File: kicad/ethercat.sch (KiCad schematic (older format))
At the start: 94 parts, among them J401 RJHSE-5384, J402 RJHSE-5384, U401 CAT24C16WI, U402 DP83822, U403 DP83822

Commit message: changing single row terminal block to double row
I've changed to double row all the connectors, RJ45 and terminal blocks,
I saves spaces and also make it more intuitive related to user
interface..lets go
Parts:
- removed C434, C435: 4700pF, servo:C_0603_1608Metric, symbol servo:Capacitor
- removed J401, J402: RJHSE-5384, Connector_RJ:RJ45_Amphenol_RJHSE538X, symbol servo:RJHSE-5384
- removed R443, R447, R448: 75e, Resistor_SMD:R_0603_1608Metric, symbol servo:Resistor
- removed R446: 470, Resistor_SMD:R_0603_1608Metric, symbol servo:Resistor
- removed TR401, TR402: S558-5500-25-F, Transformer_SMD:Transformer_Ethernet_HALO_TG111-MSC13, symbol servo:S558-5500-25-F
- added U404: rj45x2, servo:rj45x2_0845-2G1T-H5, symbol servo:rj45x2_0845-2G1T-H5
- R441: value 75e -> 470; ValueDisplayed 49.9 -> 470
- renumbered C417 to C414, C414 to C415, C415 to C416, C416 to C417, R444 to R445, R445 to R446
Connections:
- wire segments 418 -> 410
- no-connect marks 16 -> 8
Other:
- moved on the sheet: R445, R446

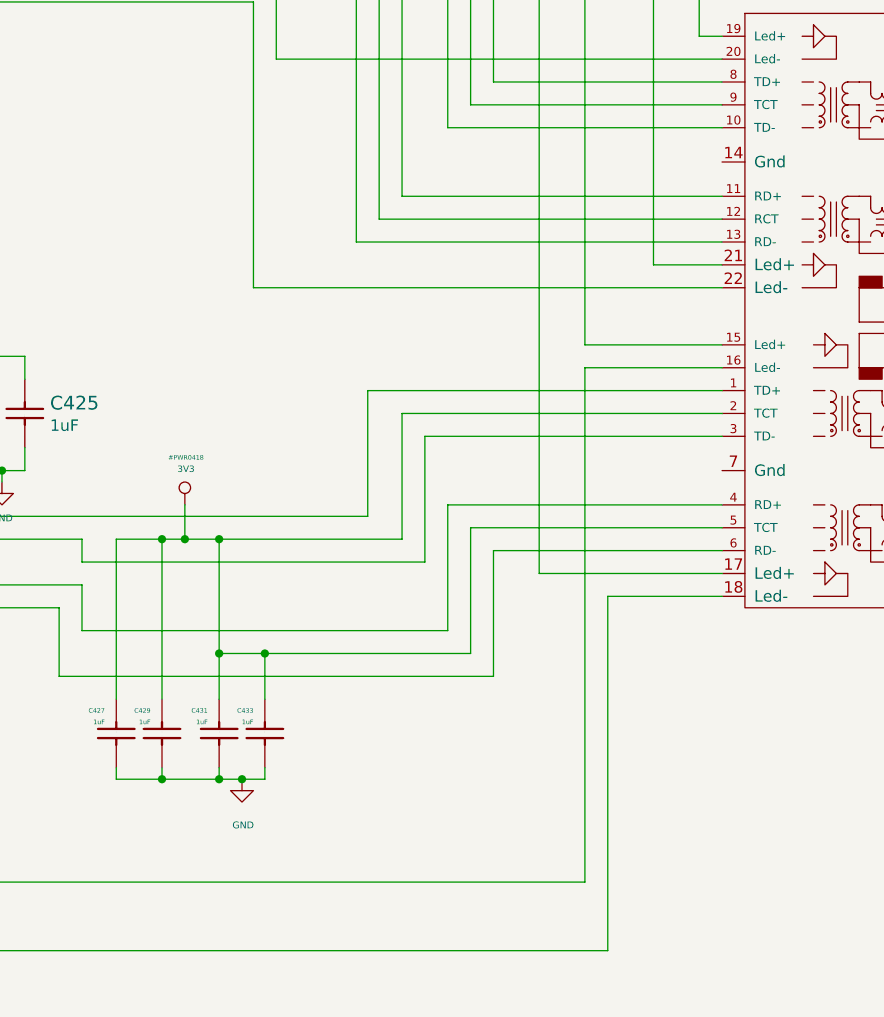
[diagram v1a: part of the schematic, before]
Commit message: added some 3d models, elminating 15vc and 2 lems
I've elminated 15vc 'cause I don't use these voltage, so I'd change 20w
15v heating power to 10w 5v more efficiency voltage to drive 3.3 and
1.2v to the core and logic. I've also elminated 2 LEMS 'cause space..
even thought there remain 3 for each motor.. more than necesary...keep
going
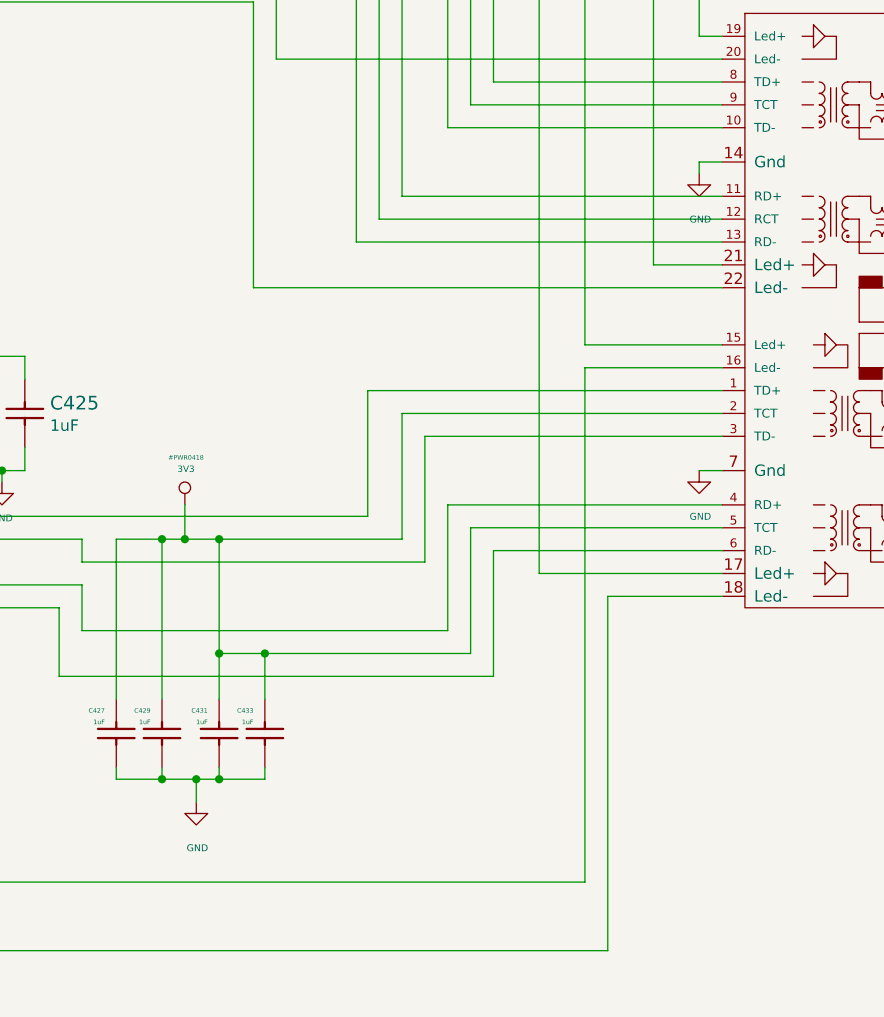
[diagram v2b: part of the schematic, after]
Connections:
- net GND: now also U404.14 (Gnd), U404.7 (Gnd)
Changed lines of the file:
@@
 L servo:GND #GND_0419
 U 1 1 6322EF1B
-P 12100 6950
-F 0 "#GND_0419" H 12105 6801 20  0001 C CNN
-F 1 "GND" H 12105 6749 30  0000 C CNN
-F 2 "" H 12100 6950 70  0000 C CNN
-F 3 "" H 12100 6950 70  0000 C CNN
-	1    12100 6950
+P 11900 7050
+F 0 "#GND_0419" H 11905 6901 20  0001 C CNN
+F 1 "GND" H 11905 6849 30  0000 C CNN
+F 2 "" H 11900 7050 70  0000 C CNN
+F 3 "" H 11900 7050 70  0000 C CNN
+	1    11900 7050
 	1    0    0    -1
 $EndComp
@@
 	2500 6100 2400 6100
 Wire Wire Line
-	12000 6950 12100 6950
-Wire Wire Line
 	12000 6400 12200 6400
 Connection ~ 12200 6400
-Connection ~ 12100 6950
-Wire Wire Line
-	12100 6950 12200 6950
-Wire Wire Line
-	12000 6950 11750 6950
+Wire Wire Line
+	12000 6950 11900 6950
 Wire Wire Line
 	11550 6950 11550 6900
@@
 Wire Wire Line
 	11150 2350 12600 2350
+Wire Wire Line
+	12000 6950 12200 6950
+Wire Wire Line
+	11900 7050 11900 6950
+Connection ~ 11900 6950
+Wire Wire Line
+	11900 6950 11750 6950
+$Comp
+L servo:GND #GND_0101
+U 1 1 5E6C77D4
+P 14100 5600
+F 0 "#GND_0101" H 14105 5451 20  0001 C CNN
+F 1 "GND" H 14105 5399 30  0000 C CNN
+F 2 "" H 14100 5600 70  0000 C CNN
+F 3 "" H 14100 5600 70  0000 C CNN
+	1    14100 5600
+	1    0    0    -1
+$EndComp
+Wire Wire Line
+	14200 5600 14100 5600
+$Comp
+L servo:GND #GND_0102
+U 1 1 5E71B6E0
+P 14100 4300
+F 0 "#GND_0102" H 14105 4151 20  0001 C CNN
+F 1 "GND" H 14105 4099 30  0000 C CNN
+F 2 "" H 14100 4300 70  0000 C CNN
+F 3 "" H 14100 4300 70  0000 C CNN
+	1    14100 4300
+	1    0    0    -1
+$EndComp
+Wire Wire Line
+	14200 4250 14100 4250
+Wire Wire Line
+	14100 4250 14100 4300
 $EndSCHEMATC

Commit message: I've reducede the PCB size ADC TVS, USB host and IDC out
TVS for ADC protection, USB out 'cause it's almost free and IDC debug
out in an IDC. Better and thinner terminal block connector help in
reduce the board size.
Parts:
- added C434: 4n7, servo:C_0603_1608Metric, symbol servo:Capacitor
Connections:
- net GND: now also C434.1; no longer U404.14 (Gnd), U404.7 (Gnd)
- new net Earth: C434.2 (Capacitor), U404.14 (Gnd), U404.7 (Gnd)
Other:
- note added: "OJO con el GND y el EARTH SPERAR"
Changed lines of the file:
@@
 Wire Wire Line
 	11900 6950 11750 6950
+Text Notes 1800 14750 0    787  ~ 157
+OJO con el GND y el EARTH SPERAR
 $Comp
-L servo:GND #GND_0101
-U 1 1 5E6C77D4
-P 14100 5600
-F 0 "#GND_0101" H 14105 5451 20  0001 C CNN
-F 1 "GND" H 14105 5399 30  0000 C CNN
-F 2 "" H 14100 5600 70  0000 C CNN
-F 3 "" H 14100 5600 70  0000 C CNN
-	1    14100 5600
+L servo:Earth #PWR?
+U 1 1 5E2B8CFA
+P 14600 6750
+AR Path="/5DC3DC9E/5E2B8CFA" Ref="#PWR?"  Part="1"
+AR Path="/5DC4A59D/5E2B8CFA" Ref="#PWR0130"  Part="1"
+F 0 "#PWR0130" H 14600 6500 20  0001 C CNN
+F 1 "Earth" H 14600 6585 39  0000 C CNN
+F 2 "" H 14600 6750 50  0001 C CNN
+F 3 "~" H 14600 6750 50  0001 C CNN
+	1    14600 6750
 	1    0    0    -1
 $EndComp
 Wire Wire Line
-	14200 5600 14100 5600
+	14000 5600 14200 5600
+Wire Wire Line
+	14000 4250 14200 4250
+$Comp
+L servo:Capacitor C434
+U 1 1 5E3BA4D2
+P 14850 6500
+F 0 "C434" V 14800 6450 20  0000 R CNN
+F 1 "4n7" V 14850 6450 20  0000 R CNN
+F 2 "servo:C_0603_1608Metric" H 14850 6400 60  0001 C CNN
+F 3 "" H 14850 6500 60  0000 C CNN
+F 4 "1uF" V 2750 7000 60  0001 C CNN "ValueDisplayed"
+	1    14850 6500
+	0    1    1    0
+$EndComp
 $Comp
 L servo:GND #GND_0102
-U 1 1 5E71B6E0
-P 14100 4300
-F 0 "#GND_0102" H 14105 4151 20  0001 C CNN
-F 1 "GND" H 14105 4099 30  0000 C CNN
-F 2 "" H 14100 4300 70  0000 C CNN
-F 3 "" H 14100 4300 70  0000 C CNN
-	1    14100 4300
+U 1 1 5E463A14
+P 14850 6750
+F 0 "#GND_0102" H 14855 6601 20  0001 C CNN
+F 1 "GND" H 14850 6593 30  0000 C CNN
+F 2 "" H 14850 6750 70  0000 C CNN
+F 3 "" H 14850 6750 70  0000 C CNN
+	1    14850 6750
 	1    0    0    -1
 $EndComp
 Wire Wire Line
-	14200 4250 14100 4250
+	14850 6750 14850 6700
 Wire Wire Line
-	14100 4250 14100 4300
+	14000 5600 14000 6400
+Wire Wire Line
+	14000 6400 14600 6400
+Wire Wire Line
+	14000 4250 14000 5600
+Connection ~ 14000 5600
+Wire Wire Line
+	14600 6750 14600 6400
+Connection ~ 14600 6400
+Wire Wire Line
+	14600 6400 14850 6400
 $EndSCHEMATC

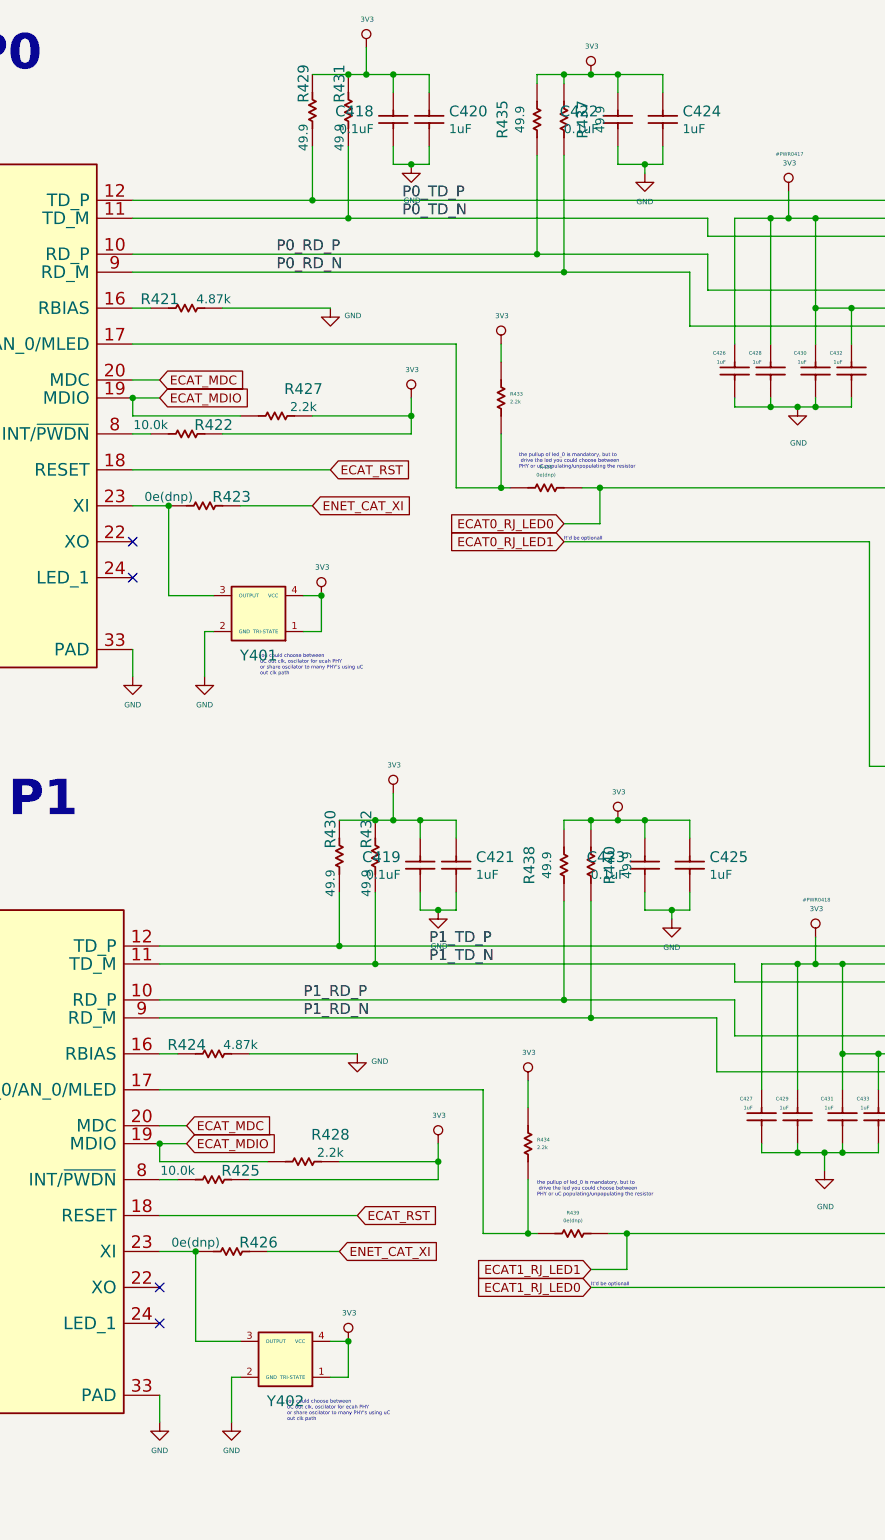
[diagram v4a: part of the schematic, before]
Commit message: placing smmall capacitors and resistors nerar his group
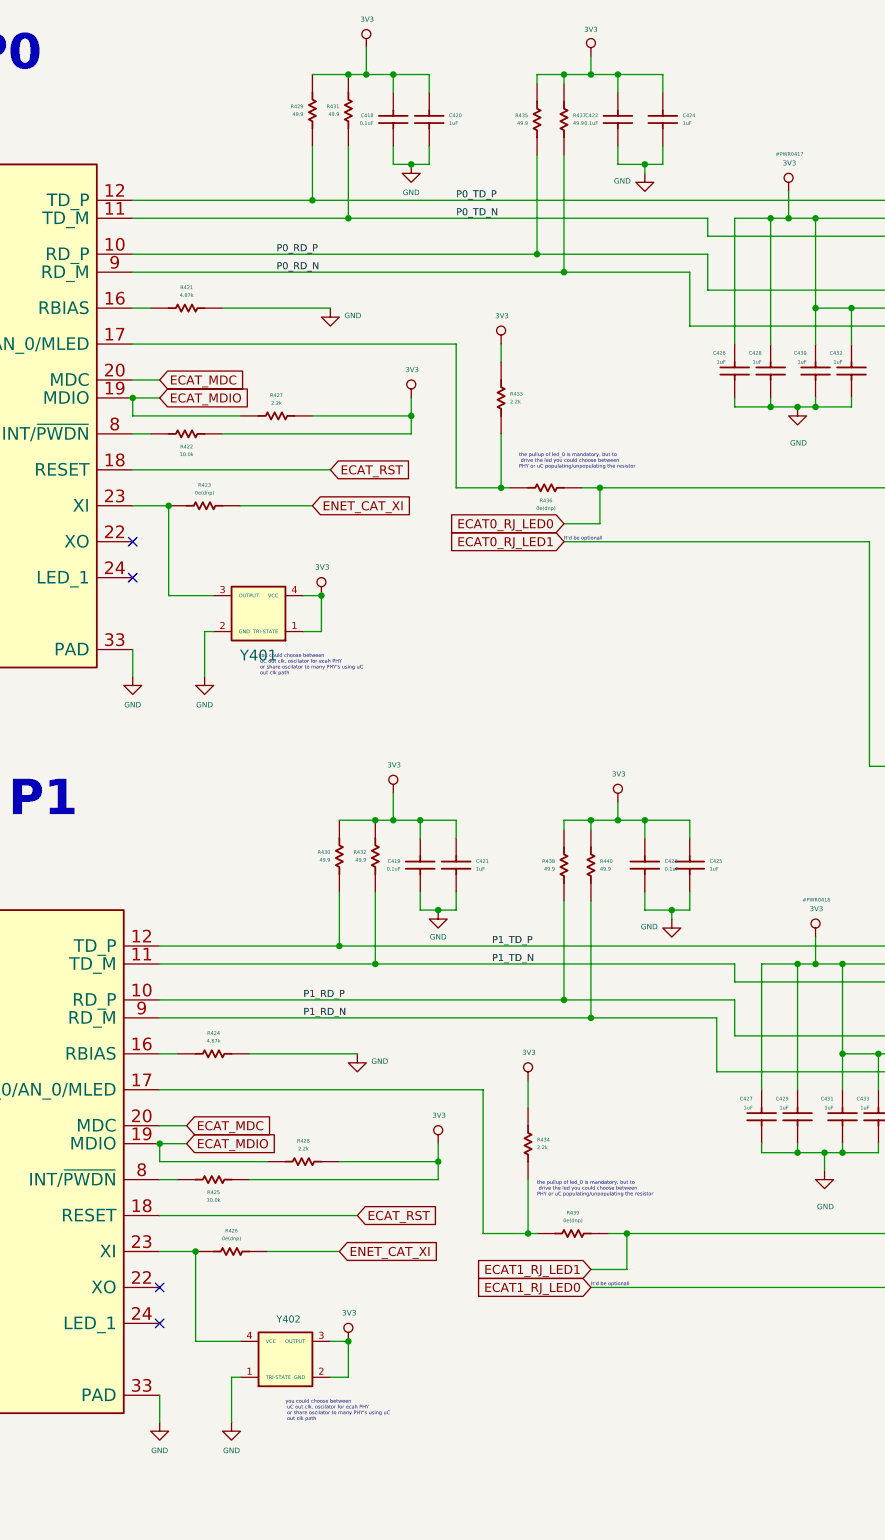
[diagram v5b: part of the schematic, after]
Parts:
- C434: footprint servo:C_0603_1608Metric -> Capacitor_SMD:C_1206_3216Metric
- U402, U403: footprint Package_DFN_QFN:QFN-32-1EP_5x5mm_P0.5mm_EP3.1x3.1mm_ThermalVias -> servo:QFN-32-1EP_5x5mm_P0.5mm_EP2.9x2.9mm_ThermalVias
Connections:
- net 3V3: now also R427.2, R428.2, R429.1, R430.1, R431.1, R432.1, R435.1, R437.1, R438.1, R440.1, Y402.2 (GND), Y402.3 (OUTPUT); no longer R427.1, R428.1, R429.2, R430.2, R431.2, R432.2, R435.2, R437.2, R438.2, R440.2, Y402.1 (TRI-STATE), Y402.4 (VCC)
- net ECAT_MDIO: now also R427.1, R428.1; no longer R427.2, R428.2
- net GND: now also Y402.1 (TRI-STATE); no longer Y402.2 (GND)
- net P0_RD_N: now also R437.2; no longer R437.1
- net P0_RD_P: now also R435.2; no longer R435.1
- net P0_TD_N: now also R431.2; no longer R431.1
- net P0_TD_P: now also R429.2; no longer R429.1
- net P1_RD_N: now also R440.2; no longer R440.1
- net P1_RD_P: now also R438.2; no longer R438.1
- net P1_TD_N: now also R432.2; no longer R432.1
- net P1_TD_P: now also R430.2; no longer R430.1
- net at R426.1, U403.23 (XI): now also Y402.4 (VCC); no longer Y402.3 (OUTPUT)

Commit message: All IC placed inside board size but....
I've placed all stuff on board size even thought all are in groups I've
to move the IC to route them. Let's begin
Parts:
- removed R428: 2.2k, Resistor_SMD:R_0603_1608Metric, symbol servo:Resistor
- R423, R426: value 0e(dnp) -> 0e
- Y401, Y402: value ~ -> dnp
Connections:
- net 3V3: now also R412.1, R413.1, R414.1, R415.1, R416.1, R427.1; no longer R412.2, R413.2, R414.2, R415.2, R416.2, R427.2
- net ECAT0_RX_ER: now also R415.2; no longer R415.1
- net ECAT1_RX_ER: now also R416.2; no longer R416.1
- net ECAT_MDIO: now also R427.2; no longer R427.1
- net at U402.27 (CRS/CRS_DV/LED_CFG): now also R413.2; no longer R413.1
- net at U403.27 (CRS/CRS_DV/LED_CFG): now also R414.2; no longer R414.1
- net at U403.29 (COL/PHYAD0/MLED): now also R412.2; no longer R412.1
- net ECAT_LED0 renamed ECAT_LED_RUN
- net ECAT_LED1 renamed ECAT_LED_ERR
- net ECAT_MDC renamed ECAT_MDCLK
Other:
- note added: "25Mhz!!"
- note added: "2k2 pullup as\n indicated by phy IC's"
- note added: "It's a good idea to have them on \nthese fitst stage but could be \nthrought away on next release."
- note removed: "OJO con el GND y el EARTH SPERAR"
- note removed: "There are totally optional"
- moved on the sheet: R427

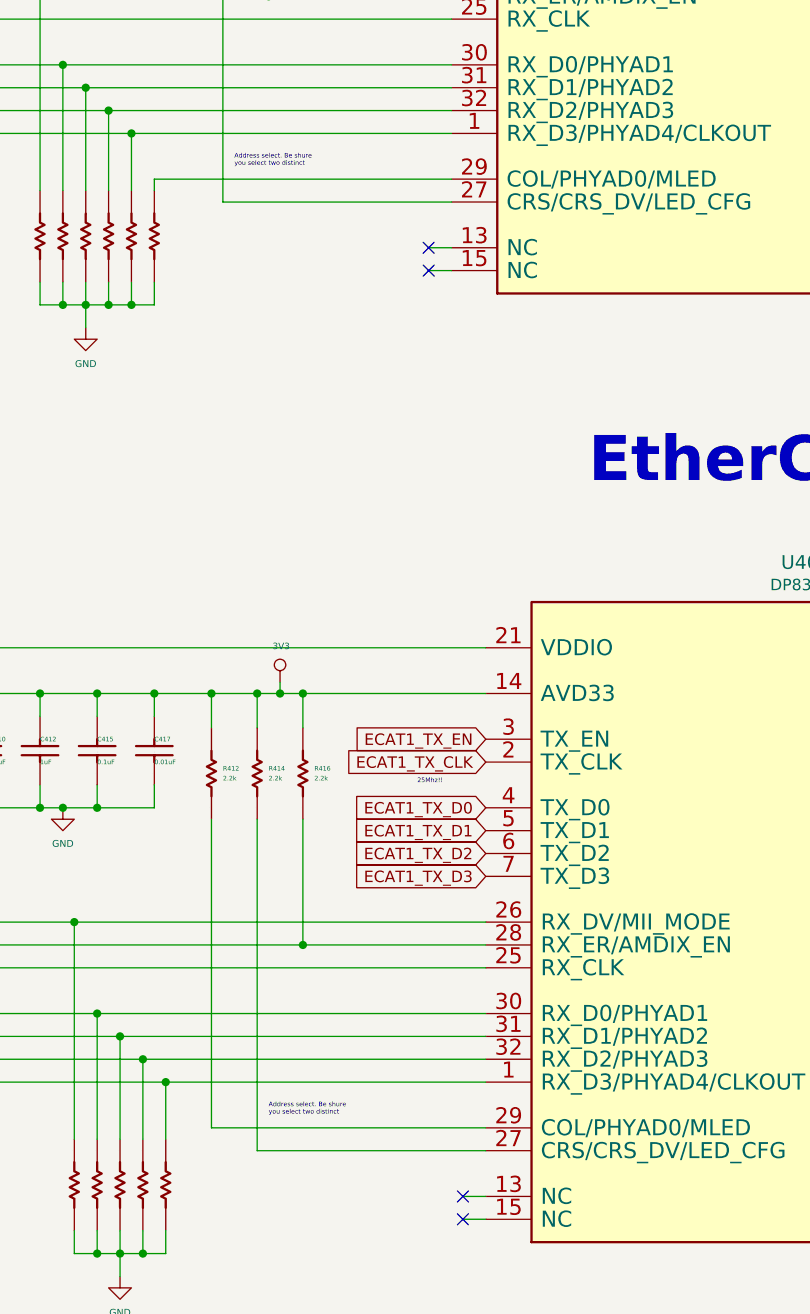
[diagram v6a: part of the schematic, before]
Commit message: mofifing ac/dc position and 3 idc out to 2
I've triung to reacomodate the ac/dc power supplies to manage isolation
and free space using 2 idc instead of 3
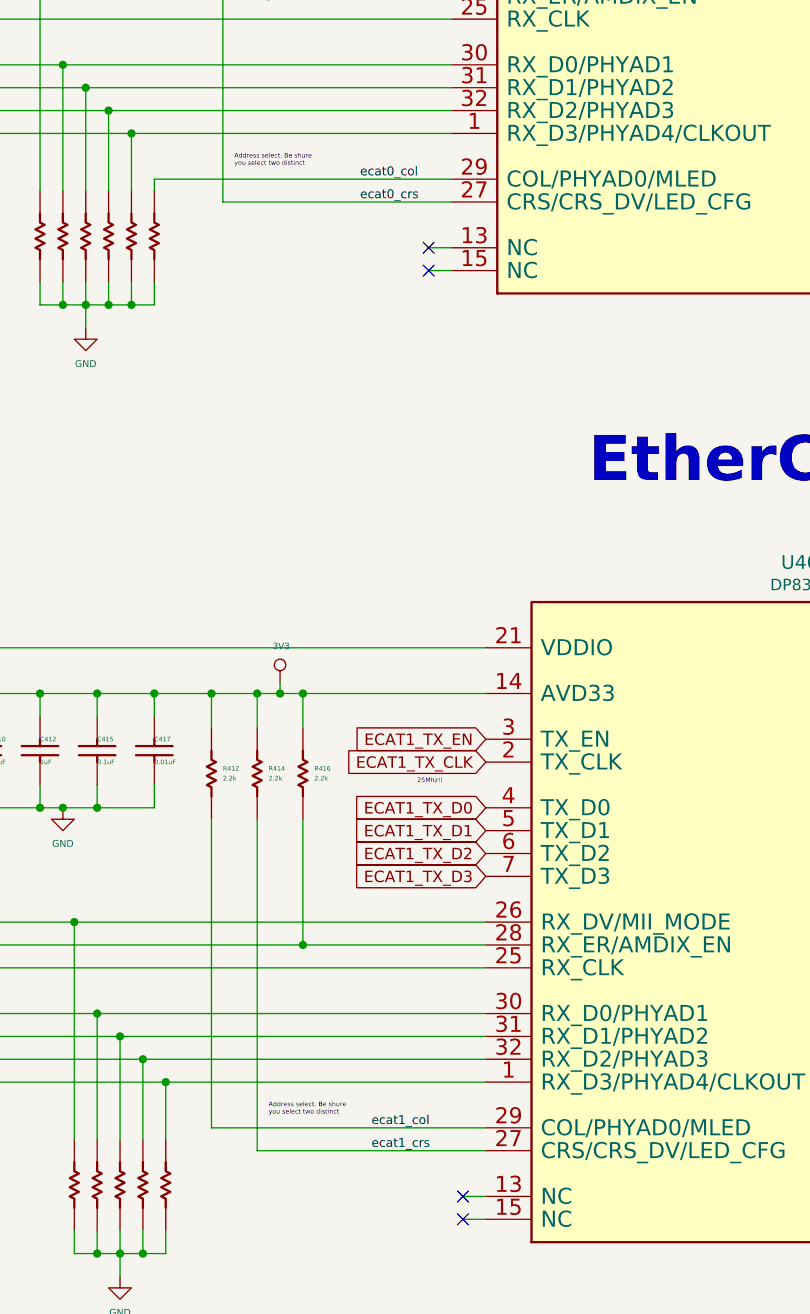
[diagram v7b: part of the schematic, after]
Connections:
- net ecat0_crs: now reaches R413.2, U402.27 (CRS/CRS_DV/LED_CFG)
- net ecat0_col: now reaches R410.2, U402.29 (COL/PHYAD0/MLED)
- net ecat1_crs: now reaches R414.2, U403.27 (CRS/CRS_DV/LED_CFG)
- net ecat1_col: now reaches R412.2, U403.29 (COL/PHYAD0/MLED)
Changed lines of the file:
@@
 Text GLabel 8350 6800 2    50   Input ~ 0
 ECAT_MDCLK
+Text Label 4850 3750 0    39   ~ 0
+ecat0_col
+Text Label 4850 3850 0    39   ~ 0
+ecat0_crs
+Text Label 4900 7900 0    39   ~ 0
+ecat1_col
+Text Label 4900 8000 0    39   ~ 0
+ecat1_crs
 $EndSCHEMATC
